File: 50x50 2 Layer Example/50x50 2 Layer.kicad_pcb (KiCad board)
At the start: 2 copper layers, 50 x 50 mm, 64 parts, among them J1 USB_C_Receptacle_USB2.0_14P, J2 Conn_01x02, J3 Conn_01x03, J5 Conn_01x02, J6 Conn_01x04, SW1 Reset, SW2 SW_SPST, U1 RP2040, U2 W25Q128JVPIQ TR, U4 Voltage Regulator, U5 DMG2305UX-7, Y1 12MHz

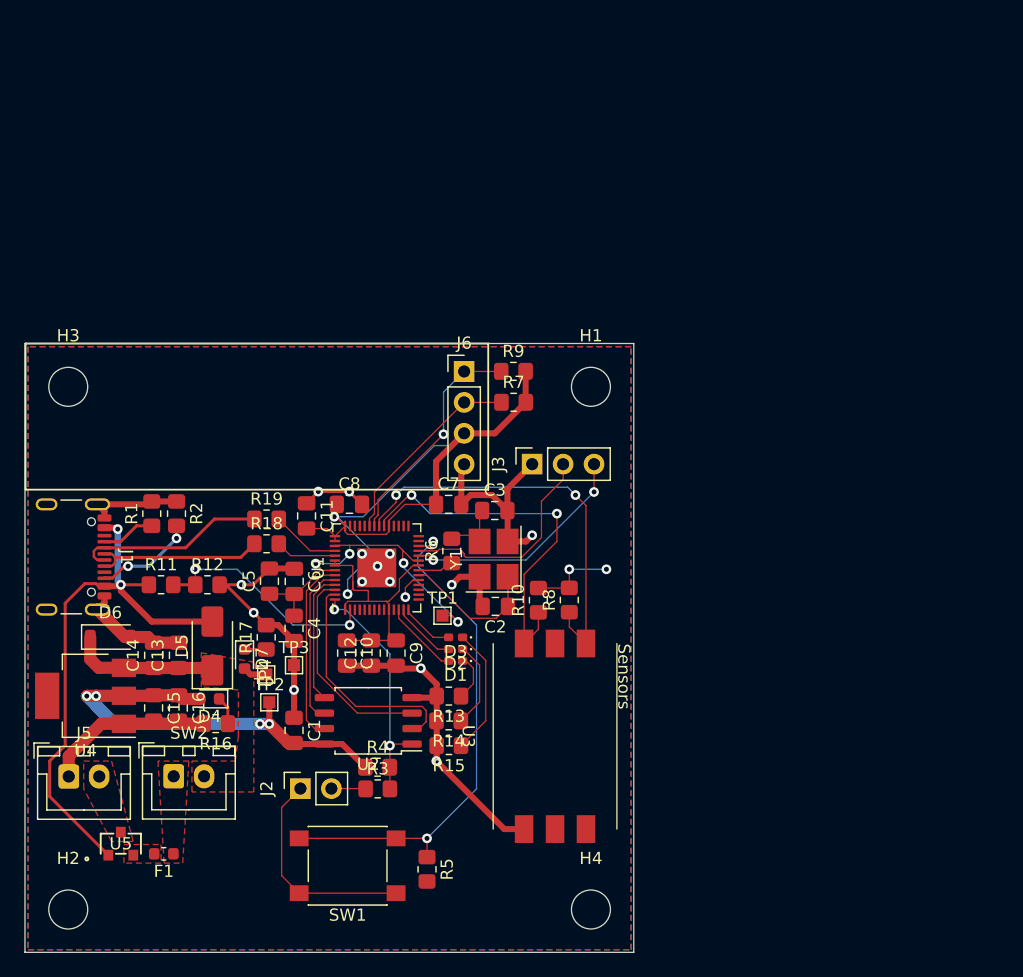
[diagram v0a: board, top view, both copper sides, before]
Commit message: Updated board and schematic
PCB and schematic have been updated to REV B
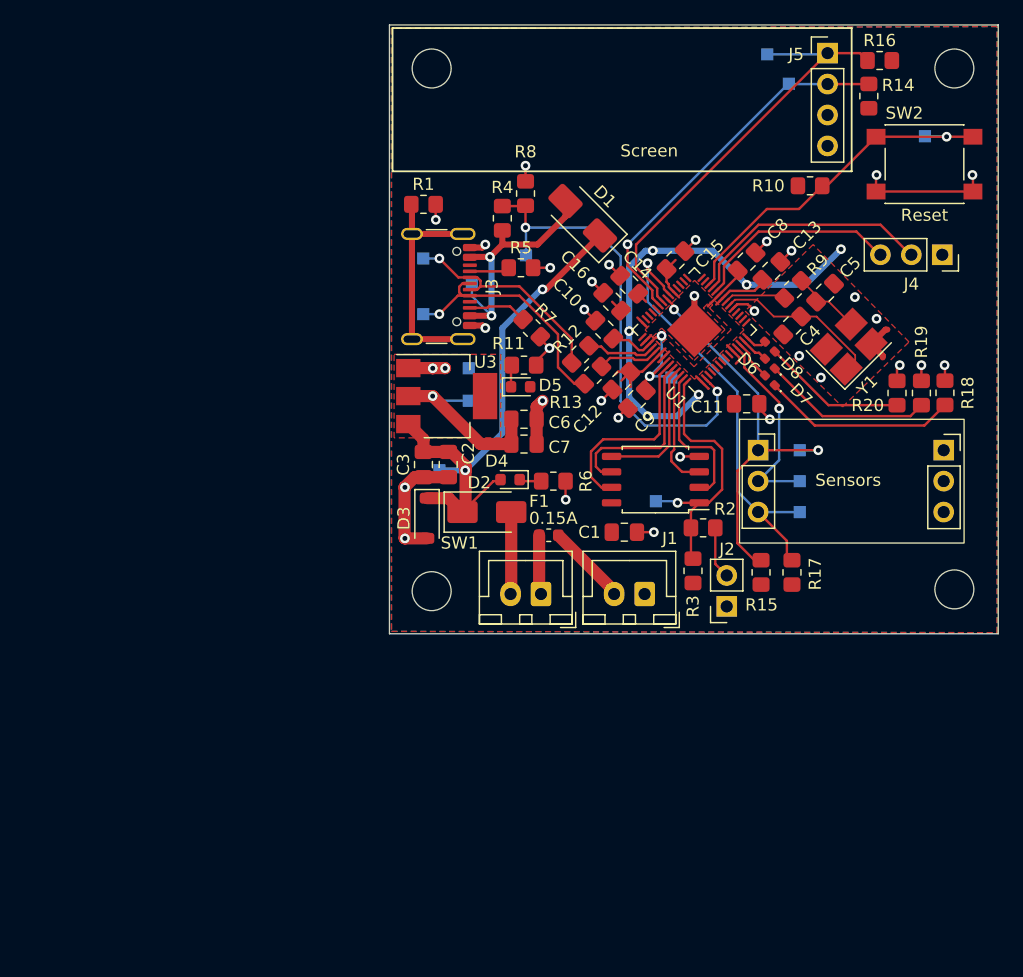
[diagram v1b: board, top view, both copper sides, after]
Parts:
- removed the J5 at (51.9, 99.1)
- removed U5: DMG2305UX-7, DMG2305UX-7:SOT-23_DIO
- added D8: LED, LED_SMD:LED_0402_1005Metric_Pad0.77x0.64mm_HandSolder, F.Cu at (109.4, 63.8)
- added J4: Conn_01x03, Connector_PinSocket_2.54mm:PinSocket_1x03_P2.54mm_Vertical, F.Cu at (123.6, 56.2)
- added R20: 130, Resistor_SMD:R_0805_2012Metric_Pad1.20x1.40mm_HandSolder, F.Cu at (119.9, 67.6)
- added TP10: 1V1, TestPoint:TestPoint_Pad_1.0x1.0mm, B.Cu at (101.3, 66.3)
- added TP11: INT_1, TestPoint:TestPoint_Pad_1.0x1.0mm, B.Cu at (111.9, 74.8)
- added TP12: I2C0_SCL, TestPoint:TestPoint_Pad_1.0x1.0mm, B.Cu at (111.0, 42.2)
- added TP13: I2C1_SCL, TestPoint:TestPoint_Pad_1.0x1.0mm, B.Cu at (111.9, 72.3)
- added TP14: I2C0_SDA, TestPoint:TestPoint_Pad_1.0x1.0mm, B.Cu at (109.2, 39.8)
- added TP15: I2C1_SDA, TestPoint:TestPoint_Pad_1.0x1.0mm, B.Cu at (111.9, 77.3)
- added TP5: USB_BOOT, TestPoint:TestPoint_Pad_1.0x1.0mm, B.Cu at (100.1, 76.5)
- added TP6: USB_DET, TestPoint:TestPoint_Pad_1.0x1.0mm, B.Cu at (89.4, 56.3)
- added TP7: BATT, TestPoint:TestPoint_Pad_1.0x1.0mm, B.Cu at (82.3, 73.9)
- added TP8: 3V3, TestPoint:TestPoint_Pad_1.0x1.0mm, B.Cu at (84.7, 68.2)
- added TP9: RST, TestPoint:TestPoint_Pad_1.0x1.0mm, B.Cu at (122.2, 46.5)
- C10: value 100nF -> 1uF
- C11, C12, C6: value 1uF -> 100nF
- C13: value 10uF -> 100nF
- C16: value 10uF -> 1uF
- C2: value 20pF -> 10uF
- C3: value 20pF -> 100nF
- C4, C5: value 100nF -> 20pF
- C7: value 100nF -> 10uF
- D1, D2: value LED -> D_Schottky; footprint LED_SMD:LED_0402_1005Metric_Pad0.77x0.64mm_HandSolder -> Diode_SMD:D_SMA
- D3: value LED -> D_Zener; footprint LED_SMD:LED_0402_1005Metric_Pad0.77x0.64mm_HandSolder -> Diode_SMD:D_SOD-123
- D4: value Green LED -> Orange LED
- D5: value D_Schottky -> Green LED; footprint Diode_SMD:D_SMA -> LED_SMD:LED_0603_1608Metric
- D6: value D_Zener -> LED; footprint Diode_SMD:D_SOD-123 -> LED_SMD:LED_0402_1005Metric_Pad0.77x0.64mm_HandSolder
- D7: value Orange LED -> LED; footprint LED_SMD:LED_0603_1608Metric -> LED_SMD:LED_0402_1005Metric_Pad0.77x0.64mm_HandSolder
- F1: value 3A -> 0.15A
- J1: value USB_C_Receptacle_USB2.0_14P -> Conn_01x02; footprint Connector_USB:USB_C_Receptacle_GCT_USB4105-xx-A_16P_TopMnt_Horizontal -> Connector_JST:JST_XH_B2B-XH-A_1x02_P2.50mm_Vertical
- J3: value Conn_01x03 -> USB_C_Receptacle_USB2.0_14P; footprint Connector_PinSocket_2.54mm:PinSocket_1x03_P2.54mm_Vertical -> Connector_USB:USB_C_Receptacle_GCT_USB4105-xx-A_16P_TopMnt_Horizontal
- R1: value 5.1k -> 0R
- R10, R8: value 4K7 -> 10k
- R11: value 5.6k -> 360R
- R12: value 10k -> 27.4
- R13: value 130 -> 27.4
- R14, R15: value 130 -> 4K7
- R16, R17: value 360R -> 4K7
- R18, R19: value 27.4 -> 130
- R2: value 5.1k -> 1k
- R3: value 1k -> DNP
- R4: value DNP -> 5.6k
- R5: value 10k -> 5.1k
- R6: value 1k -> 470R
- R7: value 4K7 -> 5.1k
- R9: value 4K7 -> 1k
- SW1: value Reset -> SW_SPST; footprint Button_Switch_SMD:SW_SPST_PTS645 -> Connector_JST:JST_XH_B2B-XH-A_1x02_P2.50mm_Vertical
- SW2: value SW_SPST -> Reset; footprint Connector_JST:JST_XH_B2B-XH-A_1x02_P2.50mm_Vertical -> Button_Switch_SMD:SW_SPST_PTS645
- TP1: value 1V1 -> GND; moved to B.Cu
- TP2: value TestPoint -> VBUS; moved to B.Cu
- TP3: value TestPoint -> D-; moved to B.Cu
- TP4: value TestPoint -> D+; moved to B.Cu
- U3: value ~ -> Voltage Regulator; footprint Sense Board:SenseBoard -> Package_TO_SOT_SMD:SOT-223
- U4: value Voltage Regulator -> ~; footprint Package_TO_SOT_SMD:SOT-223 -> Sense Board:UCA_Sense
- moved SW2 79.6 mm to (122.1, 48.8), turned to 180 degrees
- moved R16 77.1 mm to (118.5, 40.3), turned to 0 degrees
- moved U4 65.4 mm to (116.2, 74.8), turned to 0 degrees
- moved R14 61.8 mm to (117.6, 43.2), turned to -90 degrees
- moved D6 58.1 mm to (109.4, 66.5), turned to 135 degrees
- moved C13 58.0 mm to (109.6, 57.5), turned to 45 degrees
- moved R18 57.1 mm to (123.8, 67.5), turned to 90 degrees
- moved C15 56.5 mm to (101.7, 56.6), turned to -135 degrees
- moved R19 54.8 mm to (121.9, 67.6), turned to 90 degrees
- moved C5 51.4 mm to (114.0, 59.3), turned to 45 degrees
- moved R5 50.0 mm to (89.0, 57.3), turned to 0 degrees
- moved C14 49.5 mm to (97.9, 58.7), turned to 135 degrees
- moved D7 49.5 mm to (109.4, 65.2), turned to 135 degrees
- moved C16 48.8 mm to (96.5, 60.1), turned to -45 degrees
- moved J1 48.1 mm to (99.1, 84.1), turned to 180 degrees
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- renumbered H4 to H2, H2 to H3, H3 to H4, J6 to J5
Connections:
- C10 pad 1: +3V3 -> GND
- C10 pad 2: GND -> +1V1
- C11 pad 1: GND -> +3V3
- C11 pad 2: +3V3 -> GND
- C12 pad 1: GND -> +3V3
- C12 pad 2: +3V3 -> GND
- C13 pad 1: /VBatt -> +3V3
- C14 pad 1: /VBatt -> +3V3
- C15 pad 1: +3V3 -> GND
- C15 pad 2: GND -> +3V3
- C16 pad 1: +3V3 -> GND
- C16 pad 2: GND -> +3V3
- C2 pad 1: /XIN -> +BATT
- C3 pad 1: Net-(C3-Pad1) -> +BATT
- C4 pad 1: +1V1 -> /XIN
- C5 pad 1: +1V1 -> Net-(C5-Pad1)
- C6 pad 1: GND -> +3V3
- C6 pad 2: +1V1 -> GND
- C8 pad 1: +3V3 -> +1V1
- C9 pad 1: +3V3 -> +1V1
- D1 pad 1: Net-(D1-K) -> +BATT
- D1 pad 2: /LED_RED -> VBUS
- D2 pad 1: Net-(D2-K) -> +BATT
- D2 pad 2: /LED_YELLOW -> Net-(D2-A)
- D3 pad 1: Net-(D3-K) -> +BATT
- D3 pad 2: /LED_GREEN -> GND
- D4 pad 2: +3V3 -> +BATT
- D5 pad 1: /VBatt -> Net-(D5-K)
- D5 pad 2: VBUS -> +3V3
- D6 pad 1: /VBatt -> Net-(D6-K)
- D6 pad 2: GND -> /LED_RED
- D7 pad 2: /VBatt -> /LED_YELLOW
- F1 pad 1: Net-(SW2-A) -> Net-(SW1-A)
- F1 pad 2: Net-(U5-S) -> /Battery
- R1 pad 1: Net-(J1-CC1) -> Net-(J3-SHIELD)
- R10 pad 1: I2C1_SDA -> /RUN
- R11 pad 1: VBUS -> Net-(D5-K)
- R11 pad 2: USB_DET -> GND
- R12 pad 1: USB_DET -> D-
- R12 pad 2: GND -> /USB_D-
- R13 pad 1: Net-(D1-K) -> D+
- R13 pad 2: GND -> /USB_D+
- R14 pad 1: Net-(D2-K) -> I2C0_SCL
- R14 pad 2: GND -> +3V3
- R15 pad 1: Net-(D3-K) -> I2C1_SCL
- R15 pad 2: GND -> +3V3
- R16 pad 1: Net-(D4-K) -> I2C0_SDA
- R16 pad 2: GND -> +3V3
- R17 pad 1: Net-(D7-K) -> I2C1_SDA
- R17 pad 2: GND -> +3V3
- R18 pad 1: D+ -> Net-(D6-K)
- R18 pad 2: /USB_D+ -> GND
- R19 pad 1: D- -> Net-(D7-K)
- R19 pad 2: /USB_D- -> GND
- R2 pad 1: GND -> Net-(J2-Pin_2)
- R2 pad 2: Net-(J1-CC2) -> /QSPI_SS
- R3 pad 1: Net-(J2-Pin_2) -> +3V3
- R4 pad 1: +3V3 -> VBUS
- R4 pad 2: /QSPI_SS -> USB_DET
- R5 pad 1: /RUN -> Net-(J3-CC1)
- R5 pad 2: +3V3 -> GND
- R6 pad 1: /Xout -> Net-(D4-K)
- R6 pad 2: Net-(C3-Pad1) -> GND
- R7 pad 1: I2C0_SCL -> GND
- R7 pad 2: +3V3 -> Net-(J3-CC2)
- R8 pad 1: I2C1_SCL -> USB_DET
- R8 pad 2: +3V3 -> GND
- R9 pad 1: I2C0_SDA -> /Xout
- R9 pad 2: +3V3 -> Net-(C5-Pad1)
- SW1 pad 1: GND -> Net-(SW1-A)
- SW1 pad 2: /RUN -> Net-(D2-A)
- SW2 pad 1: Net-(SW2-A) -> GND
- SW2 pad 2: /VBatt -> /RUN
- TP1 pad 1: +1V1 -> GND
- TP2 pad 1: +3V3 -> VBUS
- TP3 pad 1: GND -> D-
- TP4 pad 1: /VBatt -> D+
- U1 pad 11: /GPIO_8 -> INT_1
- U3 pad 1: +3V3 -> GND
- U3 pad 2: unconnected-(U3-Pad2) -> +3V3
- U3 pad 3: GND -> +BATT
- U3 pad 4: I2C1_SCL -> (no net)
- U4 pad 1: GND -> I2C1_SCL
- U4 pad 2: +3V3 -> INT_1
- U4 pad 3: /VBatt -> I2C1_SDA
- U4 pad 4: (no net) -> GND
- Y1 pad 3: Net-(C3-Pad1) -> Net-(C5-Pad1)
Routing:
- net GND: track 128.0 -> 66.4 mm, vias 15 -> 34
- net +3V3: track 124.5 -> 78.2 mm, vias 8 -> 7
- net +BATT: track 0.00 -> 44.5 mm, vias 0 -> 2
- net VBUS: track 45.8 -> 21.5 mm
- net USB_DET: track 18.9 -> 39.2 mm
- net Net-(J3-SHIELD): track 0.00 -> 19.5 mm
- net I2C0_SDA: track 18.8 -> 36.4 mm, vias 1 -> 0
- net INT_1: track 0.00 -> 16.6 mm, vias 0 -> 1
- net Net-(D6-K): track 0.00 -> 16.0 mm
- net I2C0_SCL: track 16.4 -> 31.4 mm, vias 0 -> 1
- net /VBatt: track 13.9 -> 0.00 mm
- net +1V1: track 29.3 -> 16.6 mm, vias 4 -> 2
- net /RUN: track 42.0 -> 29.4 mm, vias 2 -> 1
- net Net-(D7-K): track 1.78 -> 14.0 mm
- net Net-(D8-K): track 0.00 -> 11.9 mm
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- added copper zone on F.Cu, net +1V1
- added copper zone on F.Cu, net GND
- removed copper zone on F.Cu, net /Batt
- removed copper zone on F.Cu, net /VBatt
- removed copper zone on F.Cu, net Net-(SW2-A)
- removed copper zone on F.Cu, net Net-(U5-S)
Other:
- board text added: "12/04/24"
- board text added: "Power Management"
- board text added: "REV: B"
- board text added: "RP2040 MCU"
- board text added: "Screen"
- board text added: "Sensors"
- board text added: "USB C"
- board text removed: "02/04/24"
- board text removed: "REV: A"
